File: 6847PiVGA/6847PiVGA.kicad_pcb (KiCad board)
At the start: 2 copper layers, 66.3 x 57.7 mm, 51 parts, among them J1 DB15_Female_HighDensity, J2 Conn_01x06_Male, U1 MC6847, U2 AD724JRZ, U3 Pico, U4 AD813, U5 TXS0108EPW, U6 TXS0108EPW, U7 TXS0108EPW, Y1 4.433620MHz

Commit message: route out board
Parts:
- removed C11: 10uF, Capacitor_SMD:C_0805_2012Metric
- removed D1: 1N5817, Diode_SMD:D_0805_2012Metric_Pad1.15x1.40mm_HandSolder
- removed U3: Pico, Package_DIP:DIP-40_W15.24mm
- added C18: 100nF, Capacitor_SMD:C_0603_1608Metric, F.Cu at (43.7, 85.9)
- added C19: 15pF, Capacitor_SMD:C_0402_1005Metric, F.Cu at (104.9, 124.7)
- added C20: 15pF, Capacitor_SMD:C_0402_1005Metric, F.Cu at (111.3, 124.7)
- added C21: 100nF, Capacitor_SMD:C_0603_1608Metric, F.Cu at (43.7, 88.4)
- added C22: 100nF, Capacitor_SMD:C_0402_1005Metric, F.Cu at (54.6, 90.9)
- added C23: 100nF, Capacitor_SMD:C_0603_1608Metric_Pad1.08x0.95mm_HandSolder, B.Cu at (108.2, 112.9)
- added C24: 100nF, Capacitor_SMD:C_0603_1608Metric_Pad1.08x0.95mm_HandSolder, B.Cu at (109.0, 116.2)
- added C25: 1uF, Capacitor_SMD:C_0603_1608Metric_Pad1.08x0.95mm_HandSolder, B.Cu at (110.2, 112.8)
- added C26: 1uF, Capacitor_SMD:C_0402_1005Metric, F.Cu at (113.8, 111.9)
- added C27: 100nF, Capacitor_SMD:C_0402_1005Metric, F.Cu at (57.5, 90.9)
- added C28: 100nF, Capacitor_SMD:C_0402_1005Metric, F.Cu at (57.5, 92.9)
- added C29: 100nF, Capacitor_SMD:C_0402_1005Metric, F.Cu at (57.5, 94.9)
- added C30: 100nF, Capacitor_SMD:C_0402_1005Metric, F.Cu at (60.4, 87.0)
- added C31: 100nF, Capacitor_SMD:C_0402_1005Metric, F.Cu at (60.4, 89.0)
- added C32: 100nF, Capacitor_SMD:C_0402_1005Metric, F.Cu at (60.4, 90.9)
- added C33: 100nF, Capacitor_SMD:C_0402_1005Metric, F.Cu at (60.4, 92.9)
- added C34: 10uF, Capacitor_SMD:C_0805_2012Metric, F.Cu at (83.9, 84.2)
- added D2: GREEN, Diode_SMD:D_0603_1608Metric, F.Cu at (115.4, 104.5)
- added D3: 1N5817, Diode_SMD:D_0805_2012Metric_Pad1.15x1.40mm_HandSolder, F.Cu at (106.8, 89.8)
- added J3: Program, Connector_PinSocket_1.27mm:PinSocket_1x05_P1.27mm_Vertical, F.Cu at (115.2, 108.1)
- added R24: DNF, Resistor_SMD:R_0603_1608Metric, F.Cu at (43.7, 90.9)
- added R25: 1K, Resistor_SMD:R_0603_1608Metric, F.Cu at (115.6, 101.9)
- added R26: 1K, Resistor_SMD:R_0603_1608Metric, F.Cu at (108.8, 120.4)
- added U10: RP2040, Package_DFN_QFN:QFN-56-1EP_7x7mm_P0.4mm_EP3.2x3.2mm, F.Cu at (108.4, 114.5)
- added U8: AMS1117-3.3, Package_TO_SOT_SMD:SOT-89-3, F.Cu at (106.7, 94.9)
- added U9: W25Q128JVS, Package_SO:SOIC-8_5.23x5.23mm_P1.27mm, F.Cu at (107.5, 103.4)
- added Y2: 12MHz, Oscillator:Oscillator_SMD_Abracon_ASE-4Pin_3.2x2.5mm_HandSoldering, F.Cu at (108.1, 123.4)
- R23: moved to F.Cu
- moved C12 13.0 mm to (92.2, 103.9), turned to -90 degrees
- moved R3 12.4 mm to (116.7, 114.0)
- moved R2 11.5 mm to (116.7, 116.0)
- moved R1 10.6 mm to (116.7, 118.0)
- moved R10 9.22 mm to (116.7, 112.0), turned to 180 degrees
- moved R6 8.51 mm to (116.7, 122.0)
- moved R5 7.73 mm to (116.7, 124.0)
- moved R9 7.04 mm to (116.7, 130.1)
- moved R4 7.04 mm to (116.7, 126.0)
- moved R8 6.44 mm to (116.7, 132.1)
- moved C3 6.24 mm to (126.2, 131.0)
- moved R7 5.97 mm to (116.7, 134.1)
- moved C2 4.96 mm to (127.5, 133.3)
- moved R11 4.77 mm to (116.7, 120.1), turned to 180 degrees
- moved C4 4.27 mm to (123.3, 112.2)
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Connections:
- C12 pad 1: OE -> +3.3V
- C13 pad 1: OE -> +3.3V
- C15 pad 1: OE -> +3.3V
- R1 pad 2: Net-(U3-GPIO26_ADC0) -> R0
- R2 pad 2: Net-(U3-GPIO27_ADC1) -> R1
- R23 pad 1: OE -> +3.3V
- R23 pad 2: GND -> OE
- R3 pad 2: Net-(U3-GPIO28_ADC2) -> R2
- R4 pad 2: Net-(U3-GPIO20) -> G0
- R5 pad 2: Net-(U3-GPIO21) -> G1
- R6 pad 2: Net-(U3-GPIO22) -> G2
- R7 pad 2: Net-(U3-GPIO17) -> B0
- R8 pad 2: Net-(U3-GPIO18) -> B1
- R9 pad 2: Net-(U3-GPIO19) -> B2
- U5 pad 1: DL0 -> DL5
- U5 pad 14: DD5 -> DD0
- U5 pad 15: DD4 -> DD1
- U5 pad 16: DD3 -> DD2
- U5 pad 17: DD2 -> DD3
- U5 pad 18: DD1 -> DD4
- U5 pad 2: OE -> +3.3V
- U5 pad 20: DD0 -> DD5
- U5 pad 3: DL1 -> DL4
- U5 pad 4: DL2 -> DL3
- U5 pad 5: DL3 -> DL2
- U5 pad 6: DL4 -> DL1
- U5 pad 7: DL5 -> DL0
- U6 pad 2: OE -> +3.3V
- U7 pad 2: OE -> +3.3V
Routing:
- net GND: track 430.3 -> 13.5 mm, vias 9 -> 6
- net VsyncL: track 121.2 -> 63.6 mm
- net +3.3V: track 0.00 -> 54.9 mm, vias 0 -> 2
- net HsyncL: track 112.9 -> 61.6 mm
- net +5VD: track 143.8 -> 177.9 mm, vias 10 -> 11
- net DD6: track 40.5 -> 8.92 mm
- net /rp2040/QSPI_SS: track 0.00 -> 28.4 mm
- net DD3: track 29.6 -> 3.36 mm, vias 4 -> 0
- net DL4: track 2.65 -> 24.5 mm
- net OE: track 90.9 -> 69.7 mm, vias 7 -> 5
- net CSSL: track 21.1 -> 0.00 mm
- net ~{A}/G_L: track 20.8 -> 0.00 mm, vias 2 -> 0
- net DL6: track 8.21 -> 26.7 mm, vias 1 -> 0
- net B0: track 0.00 -> 18.4 mm
- net DL5: track 3.83 -> 22.1 mm
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
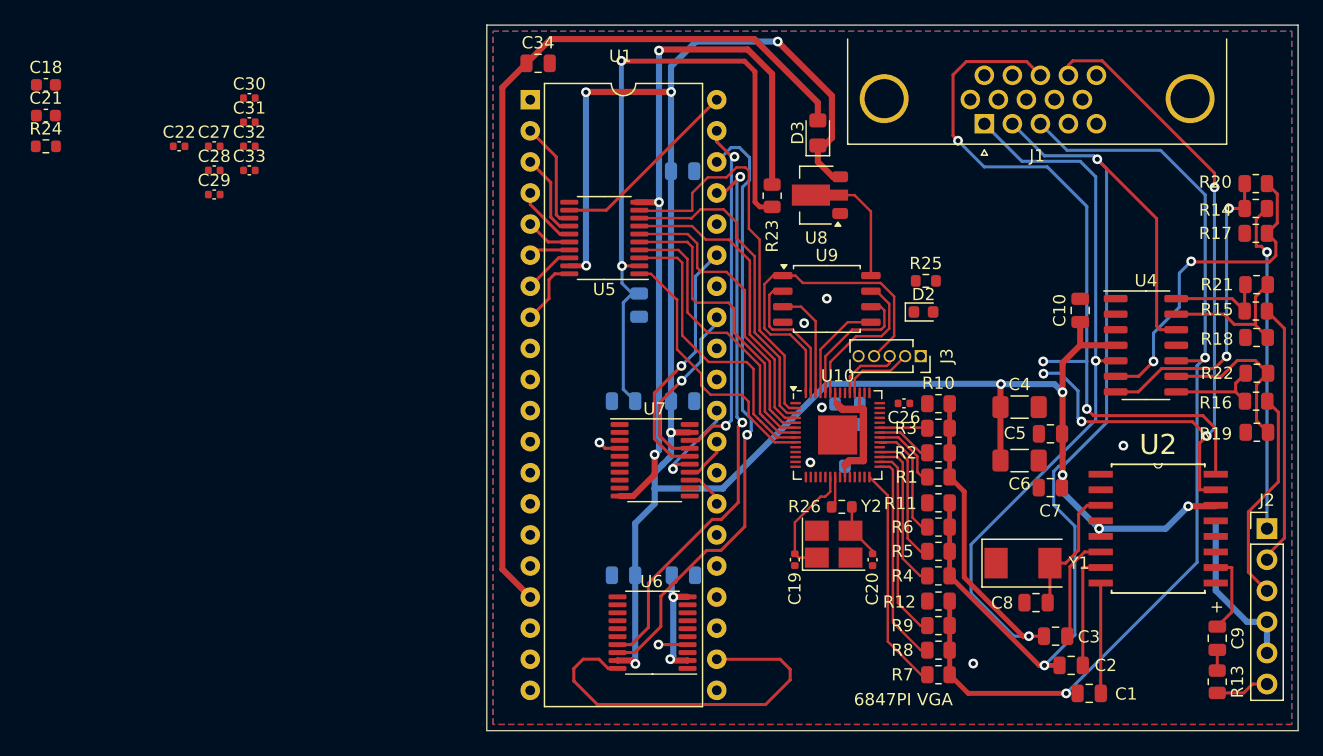
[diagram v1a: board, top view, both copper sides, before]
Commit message: complete routing
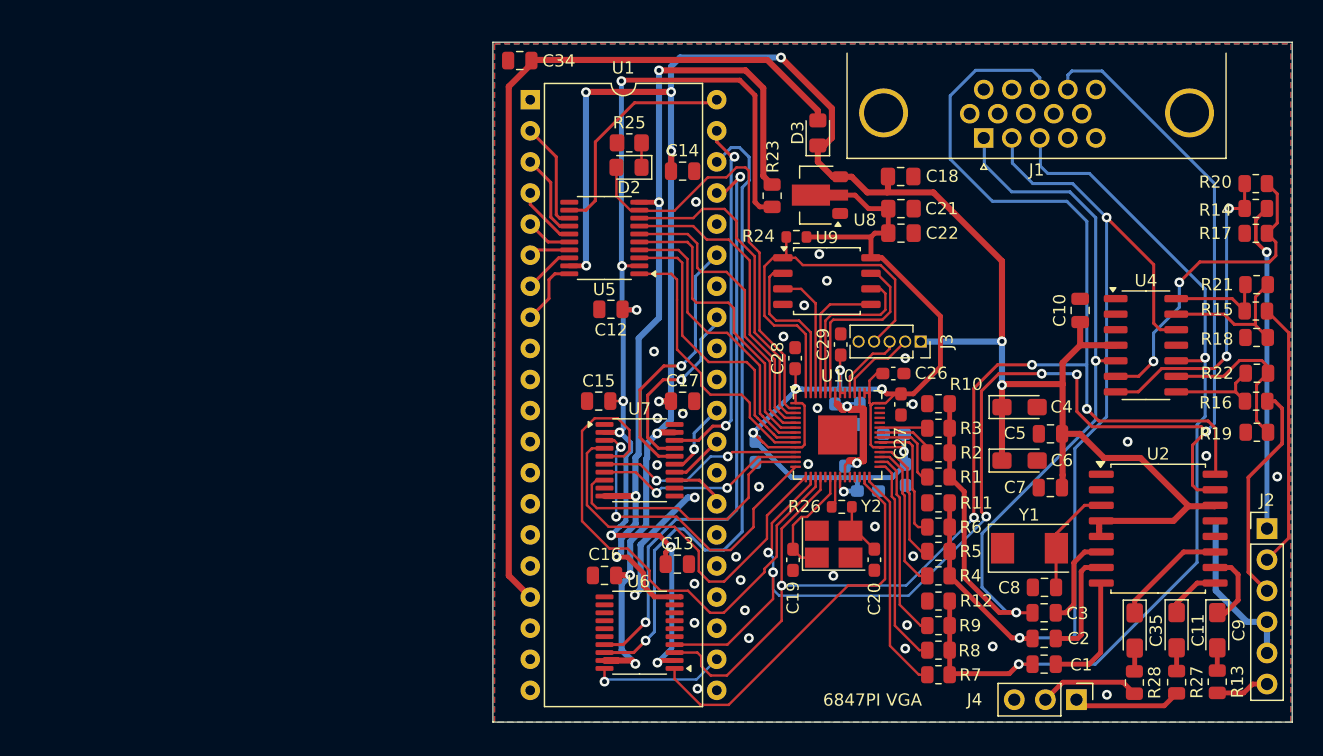
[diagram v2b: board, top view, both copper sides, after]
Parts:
- added C11: 10uF, Capacitor_Tantalum_SMD:CP_EIA-3216-10_Kemet-I_Pad1.58x1.35mm_HandSolder, F.Cu at (136.1, 130.5)
- added C35: 10uF, Capacitor_Tantalum_SMD:CP_EIA-3216-10_Kemet-I_Pad1.58x1.35mm_HandSolder, F.Cu at (132.7, 130.5)
- added J4: Conn_01x03, Connector_PinHeader_2.54mm:PinHeader_1x03_P2.54mm_Vertical, F.Cu at (127.9, 136.2)
- added R27: 75R, Resistor_SMD:R_0805_2012Metric, F.Cu at (136.1, 134.7)
- added R28: 75R, Resistor_SMD:R_0805_2012Metric, F.Cu at (132.7, 134.8)
- C12, C13, C14, C15, C16, C17: moved to F.Cu
- C18, C21: footprint Capacitor_SMD:C_0603_1608Metric -> Capacitor_SMD:C_0805_2012Metric_Pad1.18x1.45mm_HandSolder
- C19, C20, C26, C27, C28, C29: footprint Capacitor_SMD:C_0402_1005Metric -> Capacitor_SMD:C_0603_1608Metric_Pad1.08x0.95mm_HandSolder
- C22: footprint Capacitor_SMD:C_0402_1005Metric -> Capacitor_SMD:C_0805_2012Metric_Pad1.18x1.45mm_HandSolder
- C30, C31, C32, C33: footprint Capacitor_SMD:C_0402_1005Metric -> Capacitor_SMD:C_0603_1608Metric_Pad1.08x0.95mm_HandSolder; moved to B.Cu
- C4, C6: footprint Capacitor_SMD:C_1206_3216Metric_Pad1.33x1.80mm_HandSolder -> Capacitor_Tantalum_SMD:CP_EIA-3216-10_Kemet-I_Pad1.58x1.35mm_HandSolder
- C8: value 52pF -> 10pF
- C9: footprint Capacitor_SMD:C_0805_2012Metric -> Capacitor_Tantalum_SMD:CP_EIA-3216-10_Kemet-I_Pad1.58x1.35mm_HandSolder
- D2: footprint Diode_SMD:D_0603_1608Metric -> Diode_SMD:D_0805_2012Metric_Pad1.15x1.40mm_HandSolder
- R25: footprint Resistor_SMD:R_0603_1608Metric -> Resistor_SMD:R_0805_2012Metric_Pad1.20x1.40mm_HandSolder
- U2: footprint AD724JRZ:SOIC127P1032X265-16N -> Package_SO:SOIC-16W_7.5x10.3mm_P1.27mm
- moved C21 70.3 mm to (113.6, 96.0)
- moved C18 70.2 mm to (113.6, 93.4)
- moved C30 61.8 mm to (114.0, 117.8), turned to -90 degrees
- moved R24 61.8 mm to (105.1, 98.3)
- moved C27 60.0 mm to (113.6, 112.0), turned to -90 degrees
- moved C22 59.4 mm to (113.6, 98.0)
- moved C32 57.9 mm to (110.9, 119.1)
- moved C33 56.9 mm to (113.0, 114.5), turned to 180 degrees
- moved C29 52.6 mm to (108.7, 107.1), turned to 90 degrees
- moved C28 49.9 mm to (105.0, 108.2), turned to 90 degrees
- moved C31 49.3 mm to (101.7, 115.9), turned to -90 degrees
- moved D2 26.8 mm to (91.4, 92.7), turned to 180 degrees
- moved R25 26.7 mm to (91.4, 90.7)
- moved C1 4.39 mm to (125.3, 133.2)
- moved C2 3.12 mm to (125.3, 131.2)
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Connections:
- U2 pad 11: unconnected-(U2-LUMA-Pad11) -> Net-(U2-LUMA)
- U2 pad 9: unconnected-(U2-CRMA-Pad9) -> Net-(U2-CRMA)
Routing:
- net +3V3: track 8.40 -> 97.8 mm, vias 0 -> 6
- net HsyncL: track 61.6 -> 121.6 mm, vias 3 -> 4
- net VsyncL: track 63.6 -> 120.6 mm, vias 5 -> 6
- net ~{A}/G_L: track 0.00 -> 45.3 mm
- net TimingL: track 0.00 -> 32.2 mm
- net VCLKL: track 1.84 -> 31.9 mm, vias 1 -> 0
- net +3.3V: track 54.9 -> 84.4 mm, vias 2 -> 8
- net CSSL: track 0.00 -> 26.9 mm, vias 0 -> 2
- net GM2L: track 0.00 -> 22.9 mm
- net Atiming: track 31.7 -> 11.0 mm, vias 0 -> 1
- net GM1L: track 0.00 -> 17.5 mm, vias 0 -> 2
- net GM0L: track 0.00 -> 17.1 mm, vias 0 -> 2
- net +5VD: track 177.9 -> 193.7 mm
- net GND: track 13.5 -> 23.8 mm, vias 6 -> 33
- net Gvga: track 88.9 -> 78.6 mm
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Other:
- board size 66.3 x 57.7 mm -> 65.3 x 55.6 mm

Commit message: refine pcb routing
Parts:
- added R29: 100R, Resistor_SMD:R_0805_2012Metric, B.Cu at (117.7, 93.4)
- added TP1: Read/Write, TestPoint:TestPoint_Loop_D1.80mm_Drill1.0mm_Beaded, F.Cu at (119.5, 108.5)
- added TP2: E, TestPoint:TestPoint_Loop_D1.80mm_Drill1.0mm_Beaded, F.Cu at (124.1, 104.0)
- added TP3: Chip Select, TestPoint:TestPoint_Loop_D1.80mm_Drill1.0mm_Beaded, F.Cu at (119.3, 102.8)
- R1, R4, R7: value 2K 1% -> 2K2 1%
- R3, R6, R9: value 499R 1% -> 470R 1%
- moved C27 0.60 mm to (114.2, 112.0)
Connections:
- net /rp2040/GPIO29_ADC3 renamed ~{RST}
- J1 pad 13: HsyncL -> Net-(J1-Pad13)
- U10 pad 38: /rp2040/GPIO26_ADC0 -> R/~{W}
- U10 pad 39: /rp2040/GPIO27_ADC1 -> E
- U10 pad 40: /rp2040/GPIO28_ADC2 -> ~{CS}
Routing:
- net GND: track 23.8 -> 0.00 mm, vias 33 -> 38
- net E: track 0.00 -> 16.2 mm, vias 0 -> 1
- net HsyncL: track 121.6 -> 105.9 mm
- net Net-(J1-Pad13): track 0.00 -> 15.1 mm
- net ~{CS}: track 0.00 -> 13.6 mm, vias 0 -> 1
- net R/~{W}: track 0.00 -> 10.0 mm, vias 0 -> 1
- net DL2: track 25.0 -> 23.9 mm
- net DL1: track 24.8 -> 24.3 mm
- net +5VD: track 193.7 -> 193.9 mm, vias 11 -> 12

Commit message: update readme
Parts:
- added TP4: Audio, TestPoint:TestPoint_Loop_D1.80mm_Drill1.0mm_Beaded, F.Cu at (109.2, 131.0)
- J4: footprint Connector_PinHeader_2.54mm:PinHeader_1x03_P2.54mm_Vertical -> Connector_PinHeader_2.54mm:PinHeader_1x04_P2.54mm_Vertical
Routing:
- net AUDIO: track 0.00 -> 13.3 mm
- net +3V3: track 98.1 -> 96.4 mm
- net GM2L: track 22.9 -> 23.7 mm
- net GM1L: track 17.5 -> 18.3 mm
- net /rp2040/Xi: track 9.68 -> 10.3 mm
- net GND: vias 38 -> 39
